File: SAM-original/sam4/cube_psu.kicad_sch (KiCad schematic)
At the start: 17 parts, among them U3 Cube_PSM, U4 i3A4W005A150V, U5 i3A4W005A150V

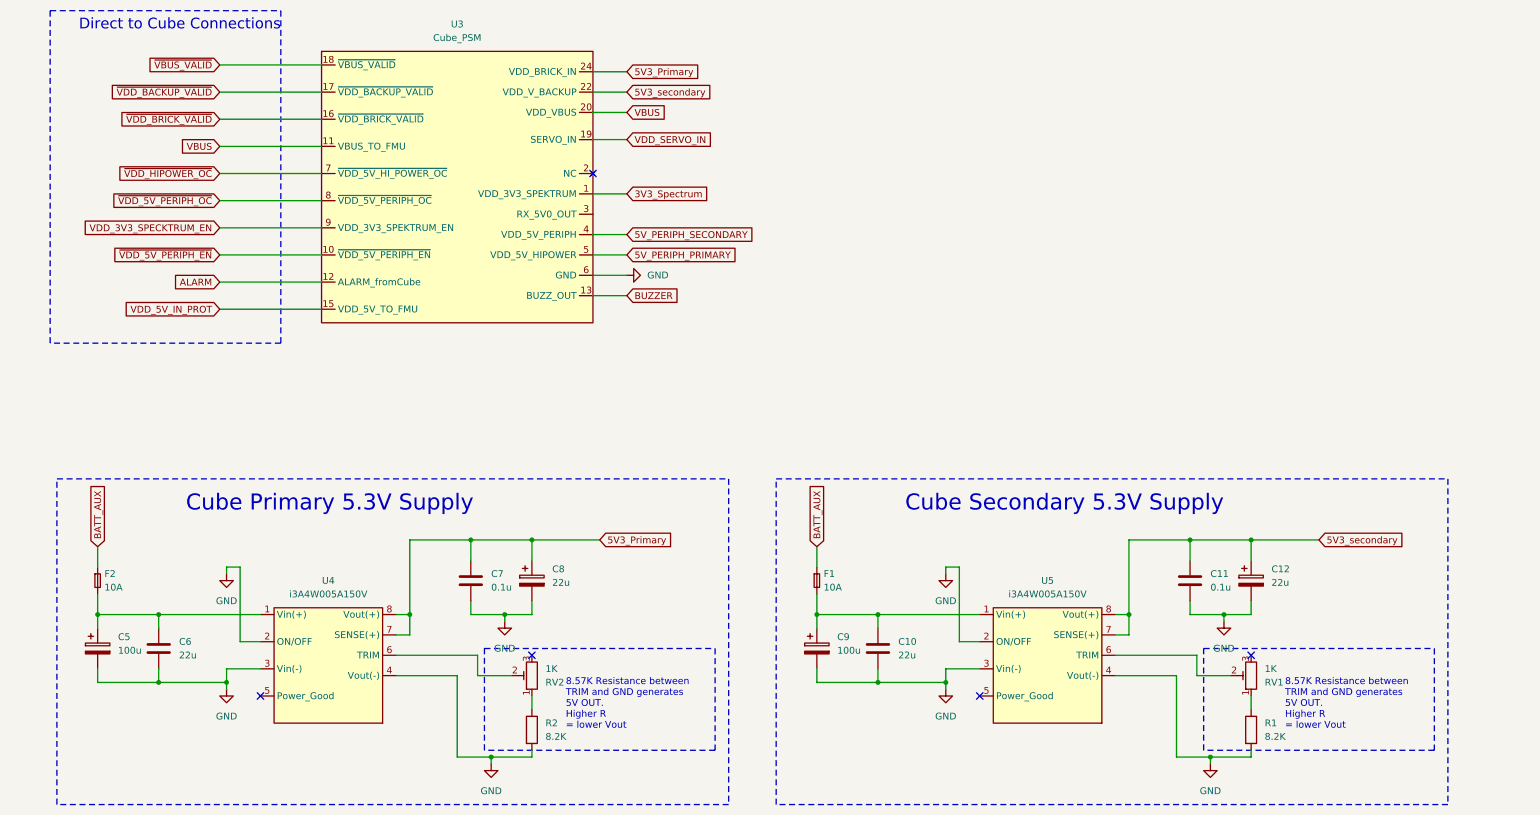
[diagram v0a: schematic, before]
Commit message: reannotate sam schem to bring into parity
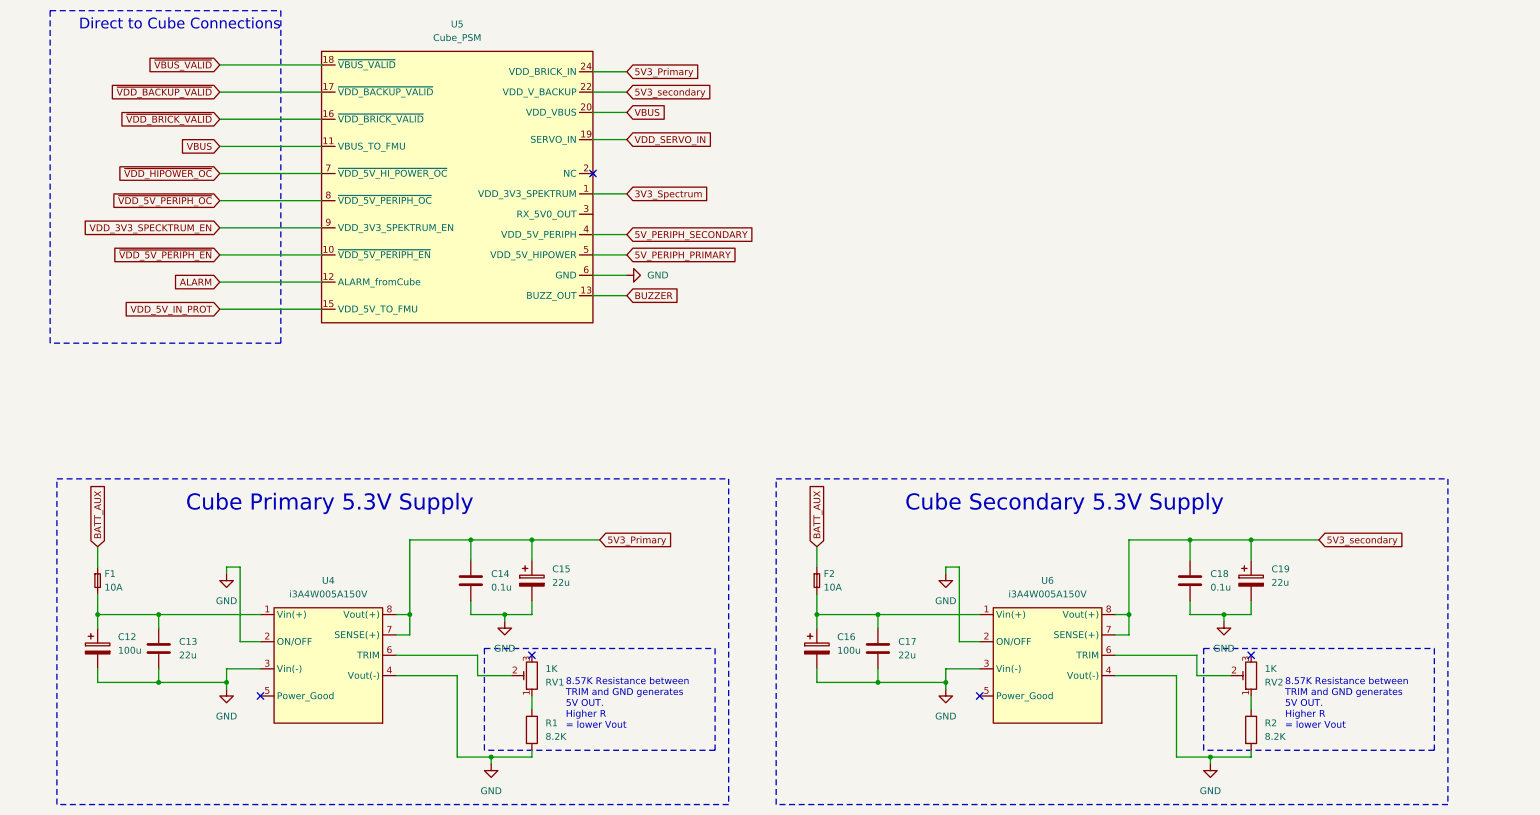
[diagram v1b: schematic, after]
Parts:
- renumbered C5 to C12, C6 to C13, C7 to C14, C8 to C15, C9 to C16, C10 to C17, C11 to C18, C12 to C19, F2 to F1, F1 to F2, R2 to R1, R1 to R2, RV2 to RV1, RV1 to RV2, U3 to U5, U5 to U6
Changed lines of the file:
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@@
 		(dnp no)
 		(fields_autoplaced yes)
-		(property "Reference" "R1"
+		(property "Reference" "R2"
 			(at 245.11 149.8599 0)
 			(effects
@@
 			(project "sam4"
 				(path "/01aa8038-f16d-42dc-9377-7a3d64116781/cd9166ba-cf56-47b5-9b6a-b5a582fcda53"
-					(reference "R1")
+					(reference "R2")
 					(unit 1)
 				)
@@
 		(dnp no)
 		(fields_autoplaced yes)
-		(property "Reference" "F1"
+		(property "Reference" "F2"
 			(at 162.56 121.9199 90)
 			(effects
@@
 			(project "sam4"
 				(path "/01aa8038-f16d-42dc-9377-7a3d64116781/cd9166ba-cf56-47b5-9b6a-b5a582fcda53"
-					(reference "F1")
+					(reference "F2")
 					(unit 1)
 				)
@@
 		(dnp no)
 		(fields_autoplaced yes)
-		(property "Reference" "C7"
+		(property "Reference" "C14"
 			(at 100.33 121.9199 0)
 			(effects
@@
 			(project "sam4"
 				(path "/01aa8038-f16d-42dc-9377-7a3d64116781/cd9166ba-cf56-47b5-9b6a-b5a582fcda53"
-					(reference "C7")
+					(reference "C14")
 					(unit 1)
 				)
@@
 		(dnp no)
 		(fields_autoplaced yes)
-		(property "Reference" "U5"
+		(property "Reference" "U6"
 			(at 204.47 123.19 0)
 			(effects
@@
 			(project "sam4"
 				(path "/01aa8038-f16d-42dc-9377-7a3d64116781/cd9166ba-cf56-47b5-9b6a-b5a582fcda53"
-					(reference "U5")
+					(reference "U6")
 					(unit 1)
 				)
@@
 		(dnp no)
 		(fields_autoplaced yes)
-		(property "Reference" "C8"
+		(property "Reference" "C15"
 			(at 111.76 121.0309 0)
 			(effects
@@
 			(project "sam4"
 				(path "/01aa8038-f16d-42dc-9377-7a3d64116781/cd9166ba-cf56-47b5-9b6a-b5a582fcda53"
-					(reference "C8")
+					(reference "C15")
 					(unit 1)
 				)
@@
 		(dnp no)
 		(fields_autoplaced yes)
-		(property "Reference" "C12"
+		(property "Reference" "C19"
 			(at 246.38 121.0309 0)
 			(effects
@@
 			(project "sam4"
 				(path "/01aa8038-f16d-42dc-9377-7a3d64116781/cd9166ba-cf56-47b5-9b6a-b5a582fcda53"
-					(reference "C12")
+					(reference "C19")
 					(unit 1)
 				)
@@
 		(dnp no)
 		(fields_autoplaced yes)
-		(property "Reference" "C5"
+		(property "Reference" "C12"
 			(at 30.48 133.7309 0)
 			(effects
@@
 			(project ""
 				(path "/01aa8038-f16d-42dc-9377-7a3d64116781/cd9166ba-cf56-47b5-9b6a-b5a582fcda53"
-					(reference "C5")
+					(reference "C12")
 					(unit 1)
 				)
@@
 		(dnp no)
 		(fields_autoplaced yes)
-		(property "Reference" "C9"
+		(property "Reference" "C16"
 			(at 165.1 133.7309 0)
 			(effects
@@
 			(project "sam4"
 				(path "/01aa8038-f16d-42dc-9377-7a3d64116781/cd9166ba-cf56-47b5-9b6a-b5a582fcda53"
-					(reference "C9")
+					(reference "C16")
 					(unit 1)
 				)
@@
 		(dnp no)
 		(fields_autoplaced yes)
-		(property "Reference" "U3"
+		(property "Reference" "U5"
 			(at 93.98 19.05 0)
 			(effects
@@
 			(project ""
 				(path "/01aa8038-f16d-42dc-9377-7a3d64116781/cd9166ba-cf56-47b5-9b6a-b5a582fcda53"
-					(reference "U3")
+					(reference "U5")
 					(unit 1)
 				)
@@
 		(dnp no)
 		(fields_autoplaced yes)
-		(property "Reference" "F2"
+		(property "Reference" "F1"
 			(at 27.94 121.9199 90)
 			(effects
@@
 			(project ""
 				(path "/01aa8038-f16d-42dc-9377-7a3d64116781/cd9166ba-cf56-47b5-9b6a-b5a582fcda53"
-					(reference "F2")
+					(reference "F1")
 					(unit 1)
 				)
@@
 		(dnp no)
 		(fields_autoplaced yes)
-		(property "Reference" "C6"
+		(property "Reference" "C13"
 			(at 41.91 134.6199 0)
 			(effects
@@
 			(project ""
 				(path "/01aa8038-f16d-42dc-9377-7a3d64116781/cd9166ba-cf56-47b5-9b6a-b5a582fcda53"
-					(reference "C6")
+					(reference "C13")
 					(unit 1)
 				)
@@
 		(dnp no)
 		(fields_autoplaced yes)
-		(property "Reference" "C10"
+		(property "Reference" "C17"
 			(at 176.53 134.6199 0)
 			(effects
@@
 			(project "sam4"
 				(path "/01aa8038-f16d-42dc-9377-7a3d64116781/cd9166ba-cf56-47b5-9b6a-b5a582fcda53"
-					(reference "C10")
+					(reference "C17")
 					(unit 1)
 				)
@@
 		(on_board yes)
 		(dnp no)
-		(property "Reference" "RV2"
+		(property "Reference" "RV1"
 			(at 110.49 142.2401 0)
 			(effects
@@
 			(project ""
 				(path "/01aa8038-f16d-42dc-9377-7a3d64116781/cd9166ba-cf56-47b5-9b6a-b5a582fcda53"
-					(reference "RV2")
+					(reference "RV1")
 					(unit 1)
 				)
@@
 		(on_board yes)
 		(dnp no)
-		(property "Reference" "RV1"
+		(property "Reference" "RV2"
 			(at 245.11 142.2401 0)
 			(effects
@@
 			(project "sam4"
 				(path "/01aa8038-f16d-42dc-9377-7a3d64116781/cd9166ba-cf56-47b5-9b6a-b5a582fcda53"
-					(reference "RV1")
+					(reference "RV2")
 					(unit 1)
 				)
@@
 		(dnp no)
 		(fields_autoplaced yes)
-		(property "Reference" "C11"
+		(property "Reference" "C18"
 			(at 234.95 121.9199 0)
 			(effects
@@
 			(project "sam4"
 				(path "/01aa8038-f16d-42dc-9377-7a3d64116781/cd9166ba-cf56-47b5-9b6a-b5a582fcda53"
-					(reference "C11")
+					(reference "C18")
 					(unit 1)
 				)
@@
 		(dnp no)
 		(fields_autoplaced yes)
-		(property "Reference" "R2"
+		(property "Reference" "R1"
 			(at 110.49 149.8599 0)
 			(effects
@@
 			(project ""
 				(path "/01aa8038-f16d-42dc-9377-7a3d64116781/cd9166ba-cf56-47b5-9b6a-b5a582fcda53"
-					(reference "R2")
-					(unit 1)
-				)
+					(reference "R1")
+					(unit 1)
+				)

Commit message: finalize core routing
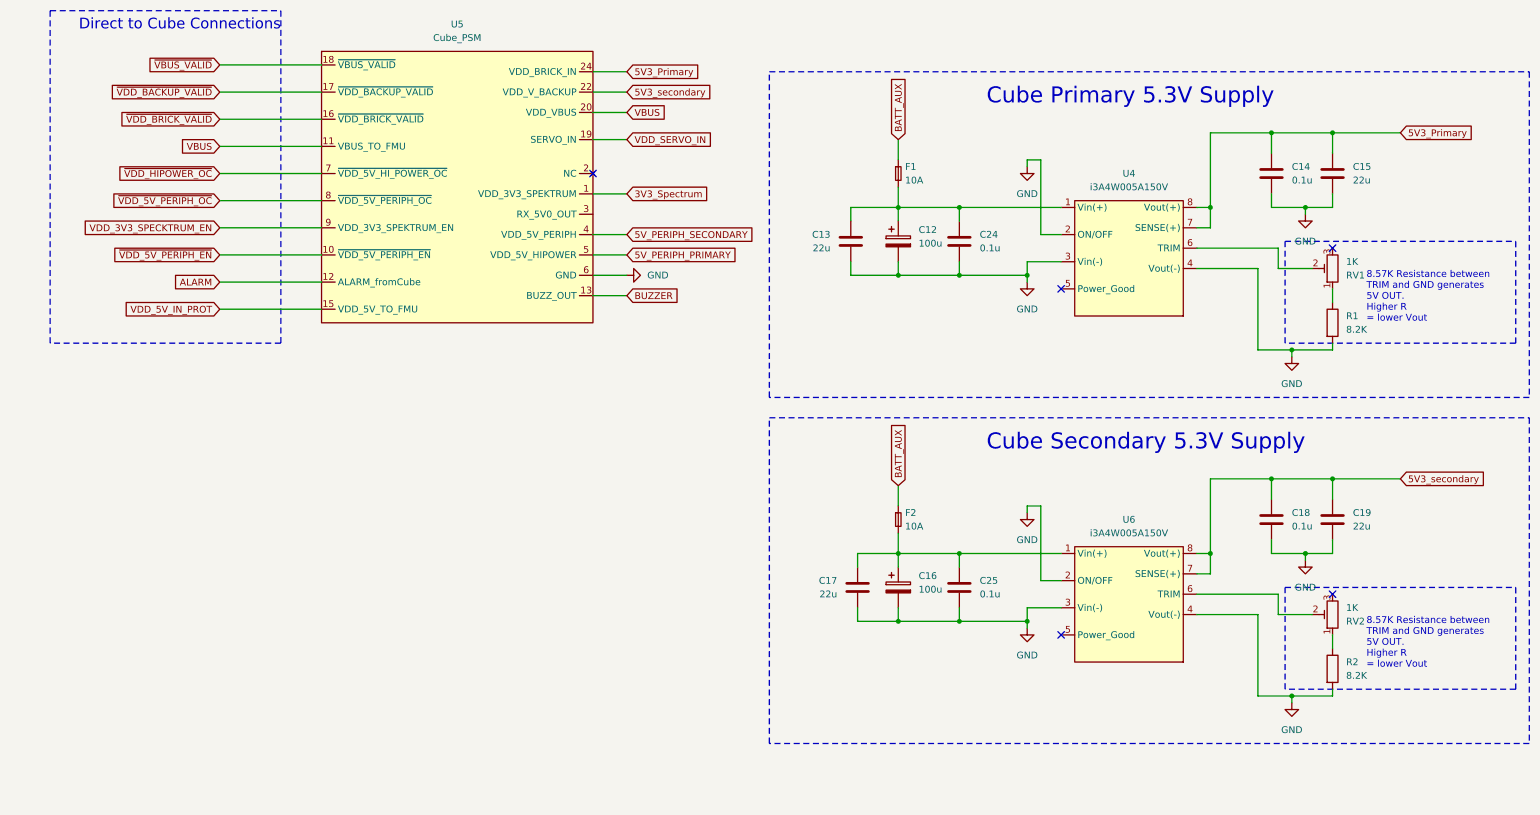
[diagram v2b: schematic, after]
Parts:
- added C24, C25: 0.1u, Capacitor_SMD:C_1206_3216Metric, symbol Device:C
- C15, C19: symbol Device:C_Polarized -> Device:C
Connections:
- net GND: now also C24.2, C25.2
- net at C16.1, C17.1, F2.2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: now also C25.1
- net at C12.1, C13.1, F1.2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: now also C24.1
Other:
- moved on the sheet: C12, C13, C14, C16, C17, C18, F1, F2, R1, R2, RV1, RV2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

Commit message: add updated SAM4 routing (DRC clean) + model
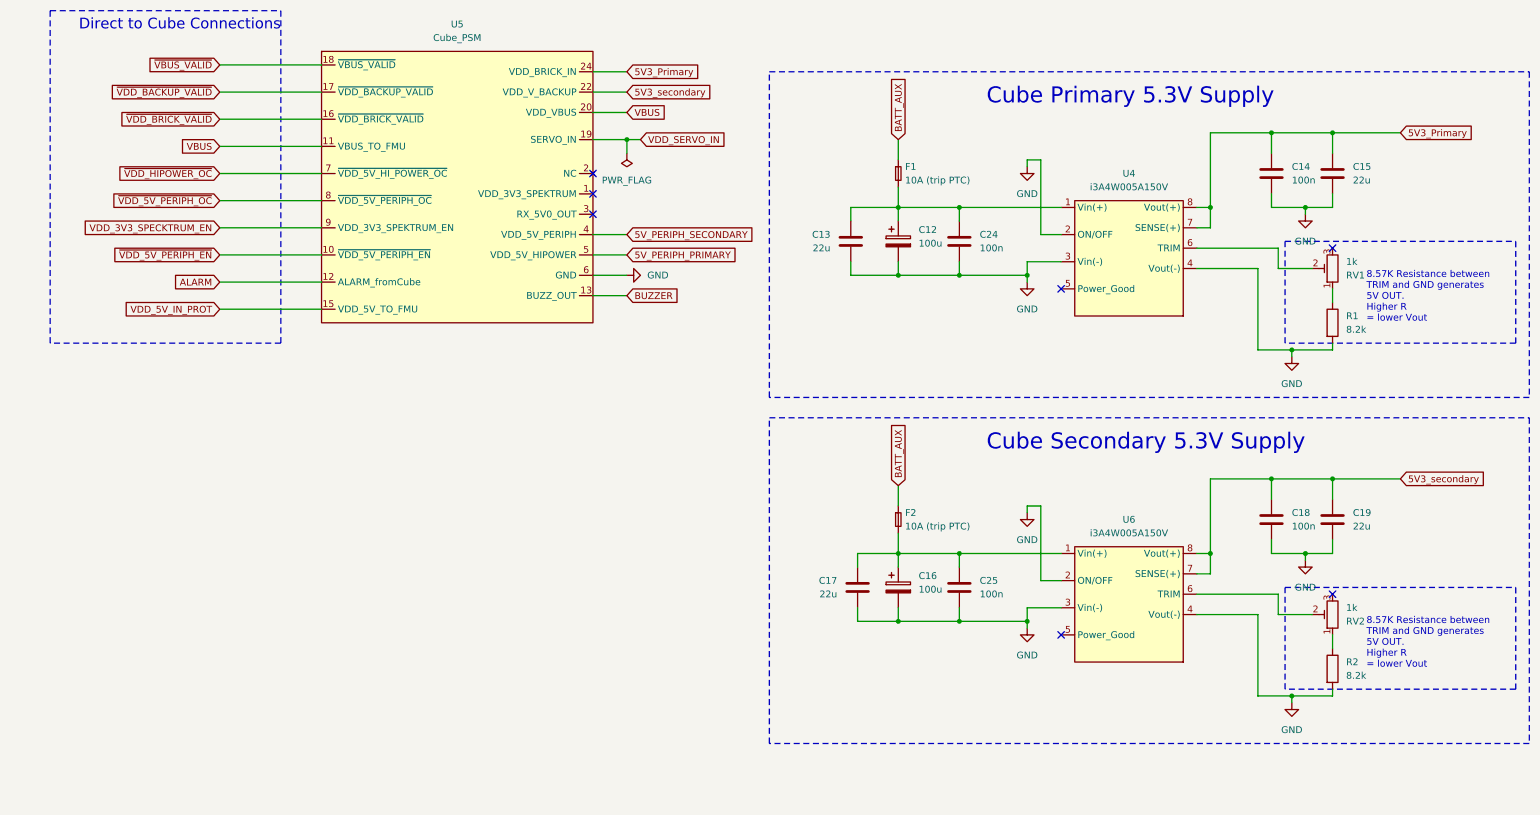
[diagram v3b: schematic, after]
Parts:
- C13, C15, C17, C19: LCSC (none) -> C12891
- C14, C18, C24, C25: value 0.1u -> 100n; LCSC (none) -> C24497
- F1, F2: value 10A -> 10A (trip PTC); footprint Fuse:Fuse_2512_6332Metric_Pad1.52x3.35mm_HandSolder -> Fuse:Fuse_1812_4532Metric_Pad1.30x3.40mm_HandSolder; LCSC (none) -> C22363547
- R1, R2: value 8.2K -> 8.2k; footprint Resistor_SMD:R_1206_3216Metric -> Resistor_SMD:R_0805_2012Metric_Pad1.20x1.40mm_HandSolder; LCSC (none) -> C17828
- RV1, RV2: value 1K -> 1k
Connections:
- net 3V3_Spectrum: no longer names the net of U5.1 (VDD_3V3_SPEKTRUM)
- no-connect marks 5 -> 7
